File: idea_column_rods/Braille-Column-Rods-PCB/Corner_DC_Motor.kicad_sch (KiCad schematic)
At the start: 9 parts, among them M9 Motor_DC_With_MP, U10 AD116, U25 MT910xET

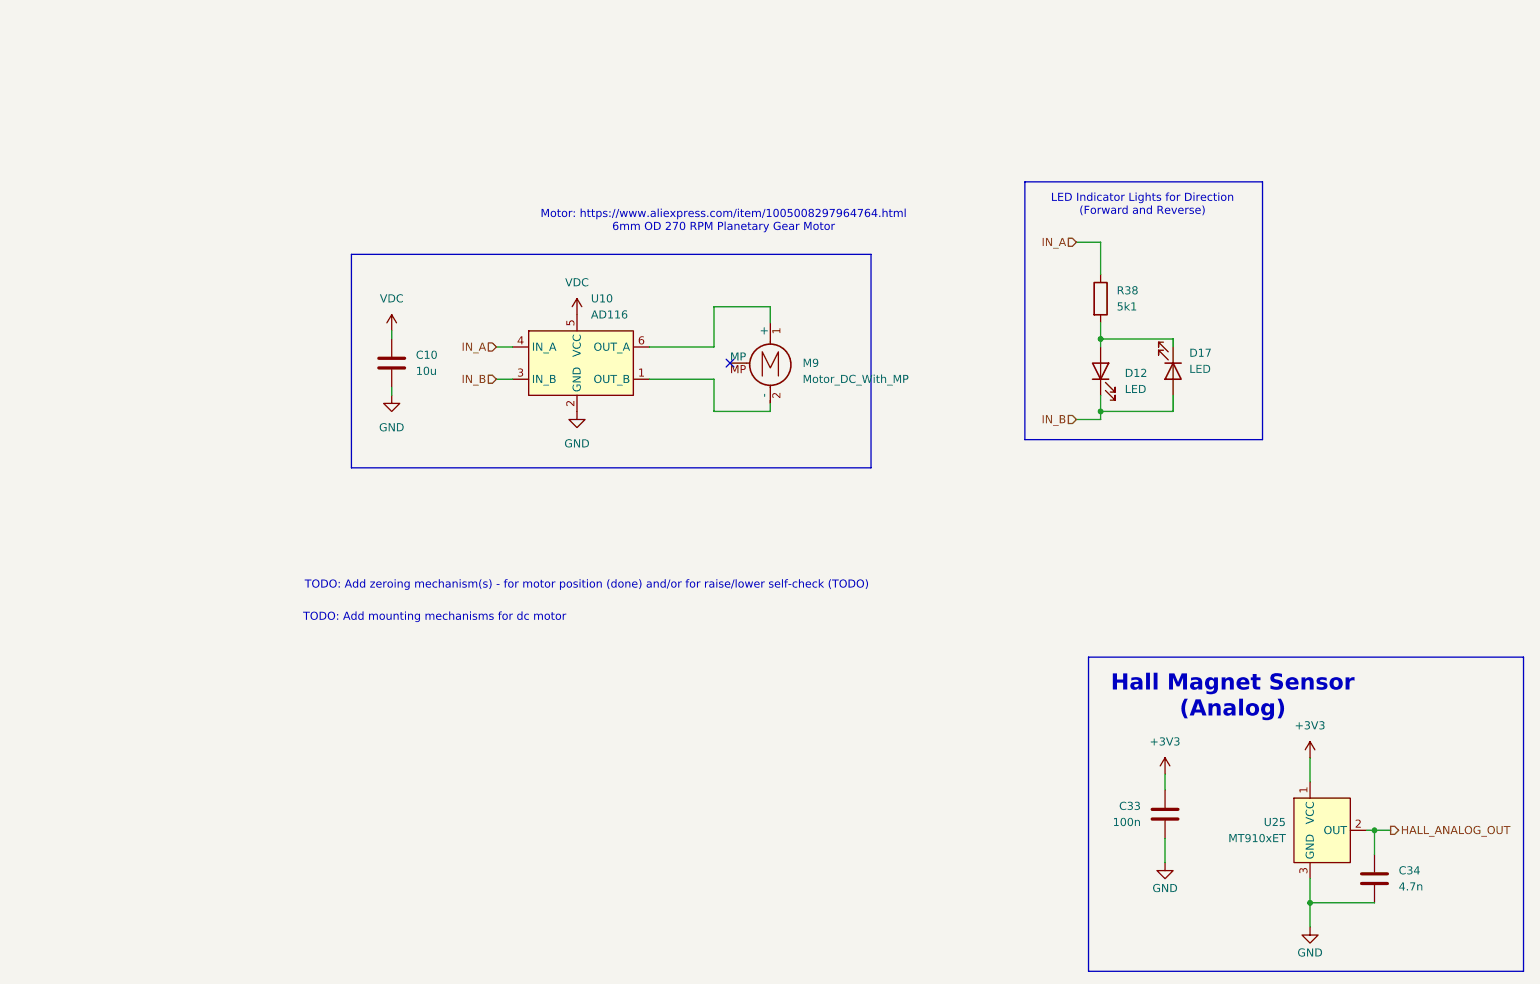
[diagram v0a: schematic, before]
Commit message: WIP: Rods PCB placement
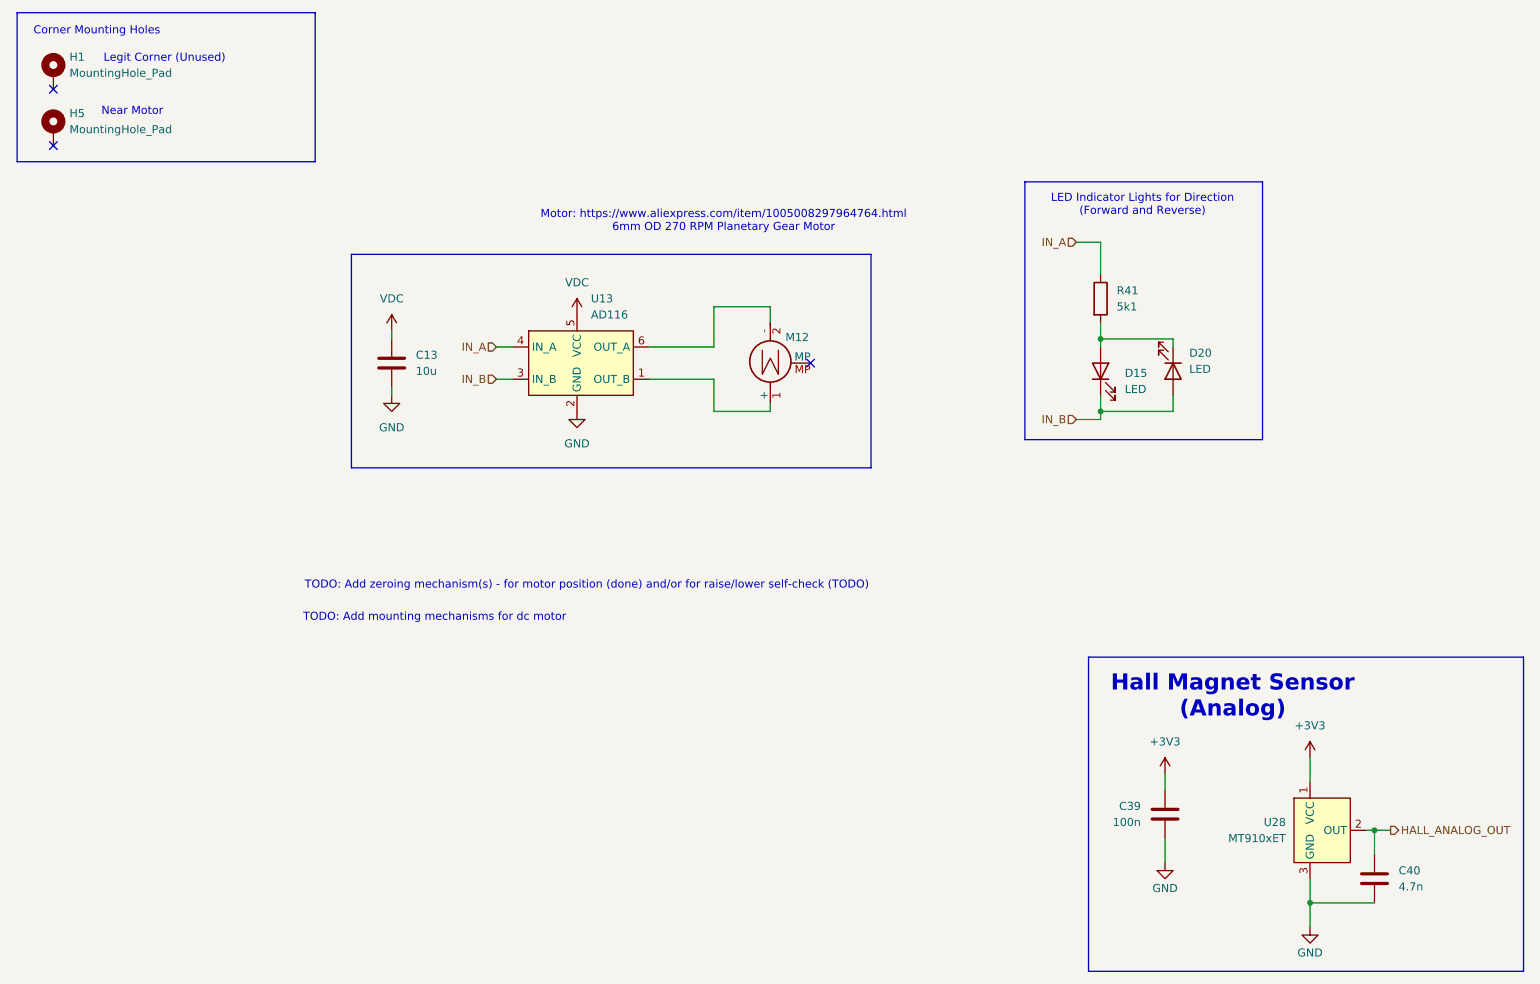
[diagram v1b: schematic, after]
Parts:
- added H1, H5: MountingHole_Pad, 00-lib-footprints:MountingHole_3.2mm_M3_Pad_NoSilk, symbol Mechanical:MountingHole_Pad
- renumbered C10 to C13, C33 to C39, C34 to C40, D12 to D15, D17 to D20, M9 to M12, R38 to R41, U10 to U13, U25 to U28
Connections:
- net at M12.1 (+): now also U13.1 (OUT_B); no longer U13.6 (OUT_A)
- net at M12.2 (-): now also U13.6 (OUT_A); no longer U13.1 (OUT_B)
- no-connect marks 1 -> 3
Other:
- note added: "Corner Mounting Holes"
- note added: "Legit Corner (Unused)"
- note added: "Near Motor"
- moved on the sheet: M12

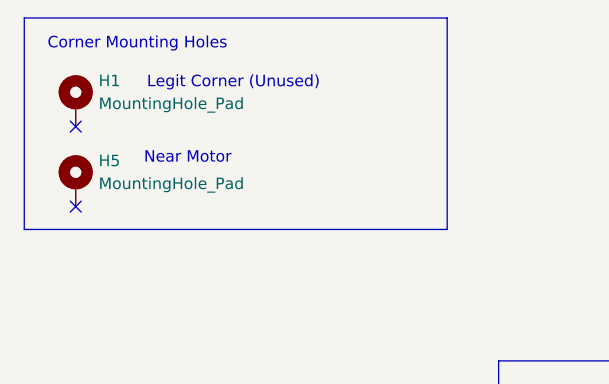
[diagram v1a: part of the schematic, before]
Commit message: WIP: Place the housing and motor X
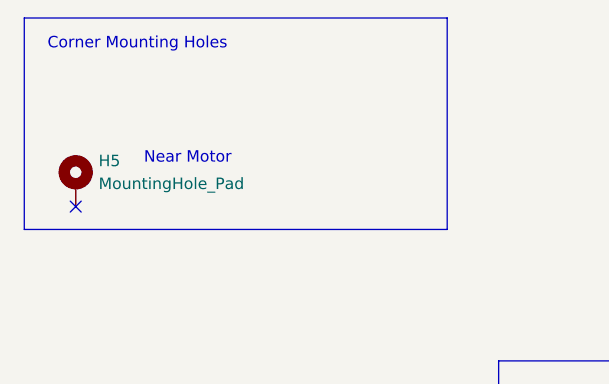
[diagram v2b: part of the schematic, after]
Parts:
- removed H1: MountingHole_Pad, 00-lib-footprints:MountingHole_3.2mm_M3_Pad_NoSilk, symbol Mechanical:MountingHole_Pad
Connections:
- no-connect marks 3 -> 2
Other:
- note removed: "Legit Corner (Unused)"
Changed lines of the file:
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@@
-	)
-	(no_connect
-		(at 24.13 27.94)
 	)
 	(no_connect
@@
 		(fill
 			(type none)
-		)
-	)
-	(text "Legit Corner (Unused)"
-		(exclude_from_sim no)
-		(at 41.656 23.114 0)
-		(effects
-			(font
-				(size 1.27 1.27)
-			)
 		)
 	)
@@
 					(unit 1)
 				)
-			)
-		)
-	)
-	(symbol
-		(lib_id "Mechanical:MountingHole_Pad")
-		(at 24.13 25.4 0)
-		(unit 1)
-		(exclude_from_sim yes)
-		(in_bom no)
-		(on_board yes)
-		(dnp no)
-		(fields_autoplaced yes)
-		(property "Reference" "H1"
-			(at 26.67 22.8599 0)
-			(effects
-				(font
-					(size 1.27 1.27)
-				)
-				(justify left)
-			)
-		)
-		(property "Value" "MountingHole_Pad"
-			(at 26.67 25.3999 0)
-			(effects
-				(font
-					(size 1.27 1.27)
-				)
-				(justify left)
-			)
-		)
-		(property "Footprint" "00-lib-footprints:MountingHole_3.2mm_M3_Pad_NoSilk"
-			(at 24.13 25.4 0)
-			(effects
-				(font
-					(size 1.27 1.27)
-				)
-				(hide yes)
-			)
-		)
-		(property "Datasheet" "~"
-			(at 24.13 25.4 0)
-			(effects
-				(font
-					(size 1.27 1.27)
-				)
-				(hide yes)
-			)
-		)
-		(property "Description" "Mounting Hole with connection"
-			(at 24.13 25.4 0)
-			(effects
-				(font
-					(size 1.27 1.27)
-				)
-				(hide yes)
-			)
-		)
-		(pin "1"
-		)
-		(instances
-			(project "Braille-Column-Rods-PCB"
-				(path "/f7fdfeea-4cd4-4338-ad68-f9089a17ed6f/1220b182-3f07-4fe8-af47-372abe179b4f/2b0fba1b-003e-4494-b9f7-98e2ce35fa03"
-					(reference "H4")
-					(unit 1)
-				)
-				(path "/f7fdfeea-4cd4-4338-ad68-f9089a17ed6f/1220b182-3f07-4fe8-af47-372abe179b4f/4a266777-439f-4c03-9f8b-0659894f2f29"
-					(reference "H2")
-					(unit 1)
-				)
-				(path "/f7fdfeea-4cd4-4338-ad68-f9089a17ed6f/1220b182-3f07-4fe8-af47-372abe179b4f/6d14cd74-7953-4982-bf48-b3d2560b5e8c"
-					(reference "H1")
-					(unit 1)
-				)
-				(path "/f7fdfeea-4cd4-4338-ad68-f9089a17ed6f/1220b182-3f07-4fe8-af47-372abe179b4f/c98a9462-365d-45ad-943d-c4627fc9b58b"
-					(reference "H3")
-					(unit 1)
-				)

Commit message: Clean up DRC (mostly footprints)
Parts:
- U28: footprint Package_TO_SOT_SMD:SOT-23 -> 00-lib-footprints:SOT-23-Hall
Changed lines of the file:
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@@
 			)
 		)
-		(property "Footprint" "Package_TO_SOT_SMD:SOT-23"
+		(property "Footprint" "00-lib-footprints:SOT-23-Hall"
 			(at 218.44 163.068 0)
 			(effects

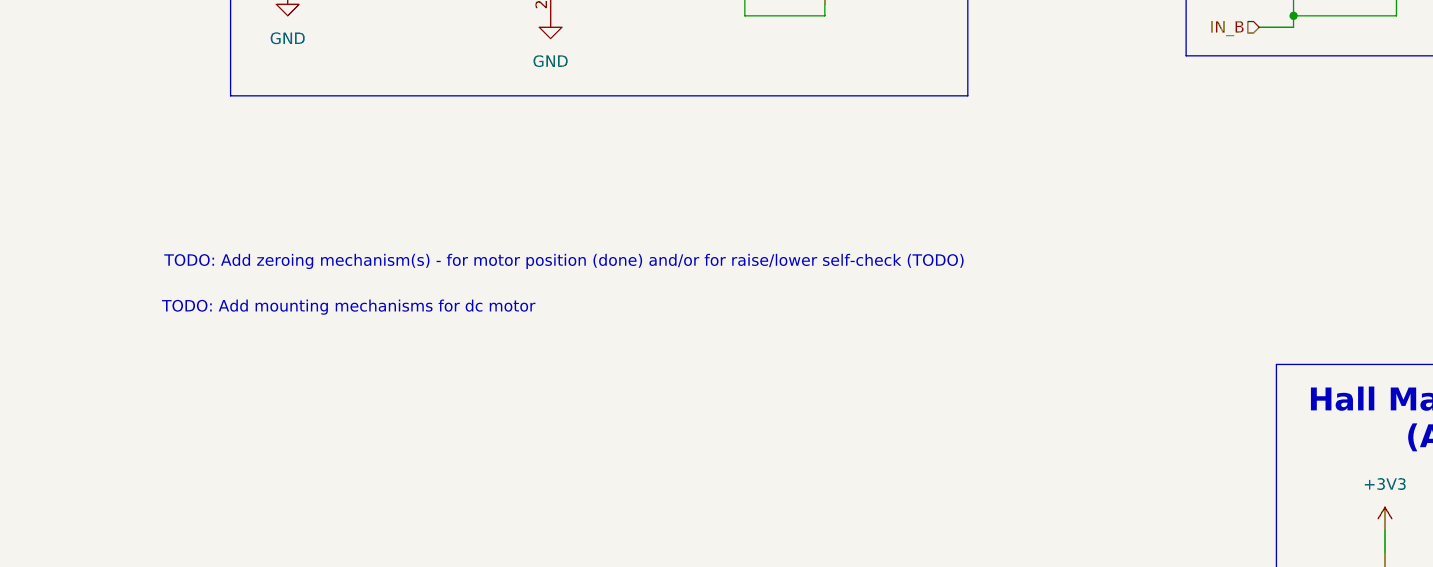
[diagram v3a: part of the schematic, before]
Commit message: Create render of 6mm motor, add to PCB
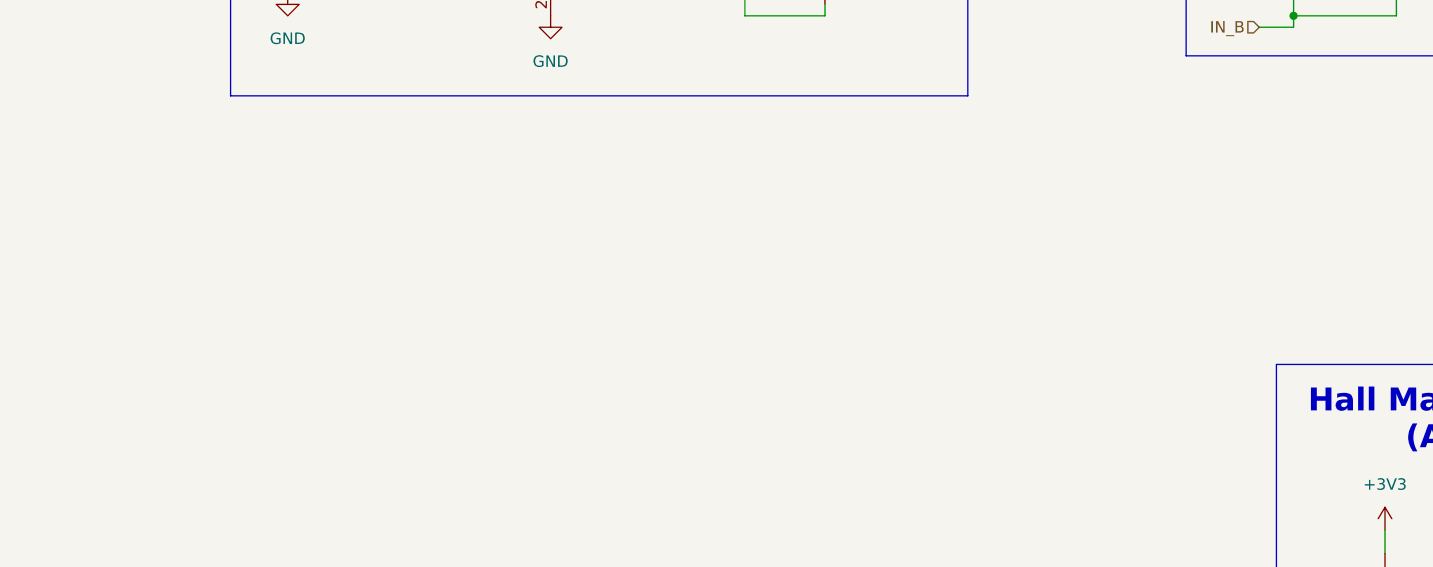
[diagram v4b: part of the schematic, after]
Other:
- note removed: "TODO: Add mounting mechanisms for dc motor"
- note removed: "TODO: Add zeroing mechanism(s) - for motor position (done) and/or for raise/lower self-check (TODO)"
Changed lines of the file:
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@@
-		)
-	)
-	(text "TODO: Add zeroing mechanism(s) - for motor position (done) and/or for raise/lower self-check (TODO)"
-		(exclude_from_sim no)
-		(at 63.754 106.172 0)
-		(effects
-			(font
-				(size 1.27 1.27)
-			)
-			(justify left)
 		)
 	)
@@
 		)
 	)
-	(text "TODO: Add mounting mechanisms for dc motor"
-		(exclude_from_sim no)
-		(at 63.5 111.252 0)
-		(effects
-			(font
-				(size 1.27 1.27)
-			)
-			(justify left)
-		)
-	)

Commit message: WIP: Get cams good
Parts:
- removed H5: MountingHole_Pad, 00-lib-footprints:MountingHole_3.2mm_M3_Pad_NoSilk, symbol Mechanical:MountingHole_Pad
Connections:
- no-connect marks 2 -> 1
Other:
- note removed: "Corner Mounting Holes"
- note removed: "Near Motor"
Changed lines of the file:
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@@
 		(at 143.51 71.12)
-	)
-	(no_connect
-		(at 24.13 36.83)
 	)
 	(wire
@@
 	)
 	(rectangle
-		(start 18.415 15.875)
-		(end 65.405 39.37)
-		(stroke
-			(width 0)
-			(type default)
-		)
-		(fill
-			(type none)
-		)
-	)
-	(rectangle
 		(start 71.12 53.975)
 		(end 153.035 87.63)
@@
 		)
 	)
-	(text "Near Motor"
-		(exclude_from_sim no)
-		(at 36.576 31.496 0)
-		(effects
-			(font
-				(size 1.27 1.27)
-			)
-		)
-	)
 	(text "Hall Magnet Sensor\n(Analog)"
 		(exclude_from_sim no)
@@
 		(exclude_from_sim no)
 		(at 129.794 48.768 0)
-		(effects
-			(font
-				(size 1.27 1.27)
-			)
-		)
-	)
-	(text "Corner Mounting Holes"
-		(exclude_from_sim no)
-		(at 30.988 18.796 0)
 		(effects
 			(font
@@
 					(unit 1)
 				)
-			)
-		)
-	)
-	(symbol
-		(lib_id "Mechanical:MountingHole_Pad")
-		(at 24.13 34.29 0)
-		(unit 1)
-		(exclude_from_sim yes)
-		(in_bom no)
-		(on_board yes)
-		(dnp no)
-		(fields_autoplaced yes)
-		(property "Reference" "H5"
-			(at 26.67 31.7499 0)
-			(effects
-				(font
-					(size 1.27 1.27)
-				)
-				(justify left)
-			)
-		)
-		(property "Value" "MountingHole_Pad"
-			(at 26.67 34.2899 0)
-			(effects
-				(font
-					(size 1.27 1.27)
-				)
-				(justify left)
-			)
-		)
-		(property "Footprint" "00-lib-footprints:MountingHole_3.2mm_M3_Pad_NoSilk"
-			(at 24.13 34.29 0)
-			(effects
-				(font
-					(size 1.27 1.27)
-				)
-				(hide yes)
-			)
-		)
-		(property "Datasheet" "~"
-			(at 24.13 34.29 0)
-			(effects
-				(font
-					(size 1.27 1.27)
-				)
-				(hide yes)
-			)
-		)
-		(property "Description" "Mounting Hole with connection"
-			(at 24.13 34.29 0)
-			(effects
-				(font
-					(size 1.27 1.27)
-				)
-				(hide yes)
-			)
-		)
-		(pin "1"
-		)
-		(instances
-			(project "Braille-Column-Rods-PCB"
-				(path "/f7fdfeea-4cd4-4338-ad68-f9089a17ed6f/1220b182-3f07-4fe8-af47-372abe179b4f/2b0fba1b-003e-4494-b9f7-98e2ce35fa03"
-					(reference "H8")
-					(unit 1)
-				)
-				(path "/f7fdfeea-4cd4-4338-ad68-f9089a17ed6f/1220b182-3f07-4fe8-af47-372abe179b4f/4a266777-439f-4c03-9f8b-0659894f2f29"
-					(reference "H6")
-					(unit 1)
-				)
-				(path "/f7fdfeea-4cd4-4338-ad68-f9089a17ed6f/1220b182-3f07-4fe8-af47-372abe179b4f/6d14cd74-7953-4982-bf48-b3d2560b5e8c"
-					(reference "H5")
-					(unit 1)
-				)
-				(path "/f7fdfeea-4cd4-4338-ad68-f9089a17ed6f/1220b182-3f07-4fe8-af47-372abe179b4f/c98a9462-365d-45ad-943d-c4627fc9b58b"
-					(reference "H7")
-					(unit 1)
-				)

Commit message: Complete type 4 rev 1
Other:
- title: (none) -> Braille Cam Rod Prototype (Type 4)
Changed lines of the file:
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@@
 	(generator_version "8.0")
 	(paper "USLetter")
+	(title_block
+		(title "Braille Cam Rod Prototype (Type 4)")
+		(date "2025-01-06")
+		(rev "Rev 1")
+	)
 	(junction
 		(at 222.25 156.21)
